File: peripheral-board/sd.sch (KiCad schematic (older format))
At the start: 0 parts

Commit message: keyboard switches and diodes placed
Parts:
- added CON7001: SD_Card, symbol SD_Card
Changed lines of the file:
@@
 $Descr A4 11693 8268
 encoding utf-8
-Sheet 1 9
+Sheet 7 9
 Title ""
 Date ""
@@
 Comment4 ""
 $EndDescr
+$Comp
+L SD_Card CON7001
+U 1 1 581F6986
+P 5750 3400
+F 0 "CON7001" H 5750 4155 50  0000 C CNN
+F 1 "SD_Card" H 5750 4064 50  0000 C CNN
+F 2 "" H 5750 3973 50  0001 C CNN
+F 3 "" H 5750 3400 50  0000 C CNN
+	1    5750 3400
+	1    0    0    -1
+$EndComp
 $EndSCHEMATC

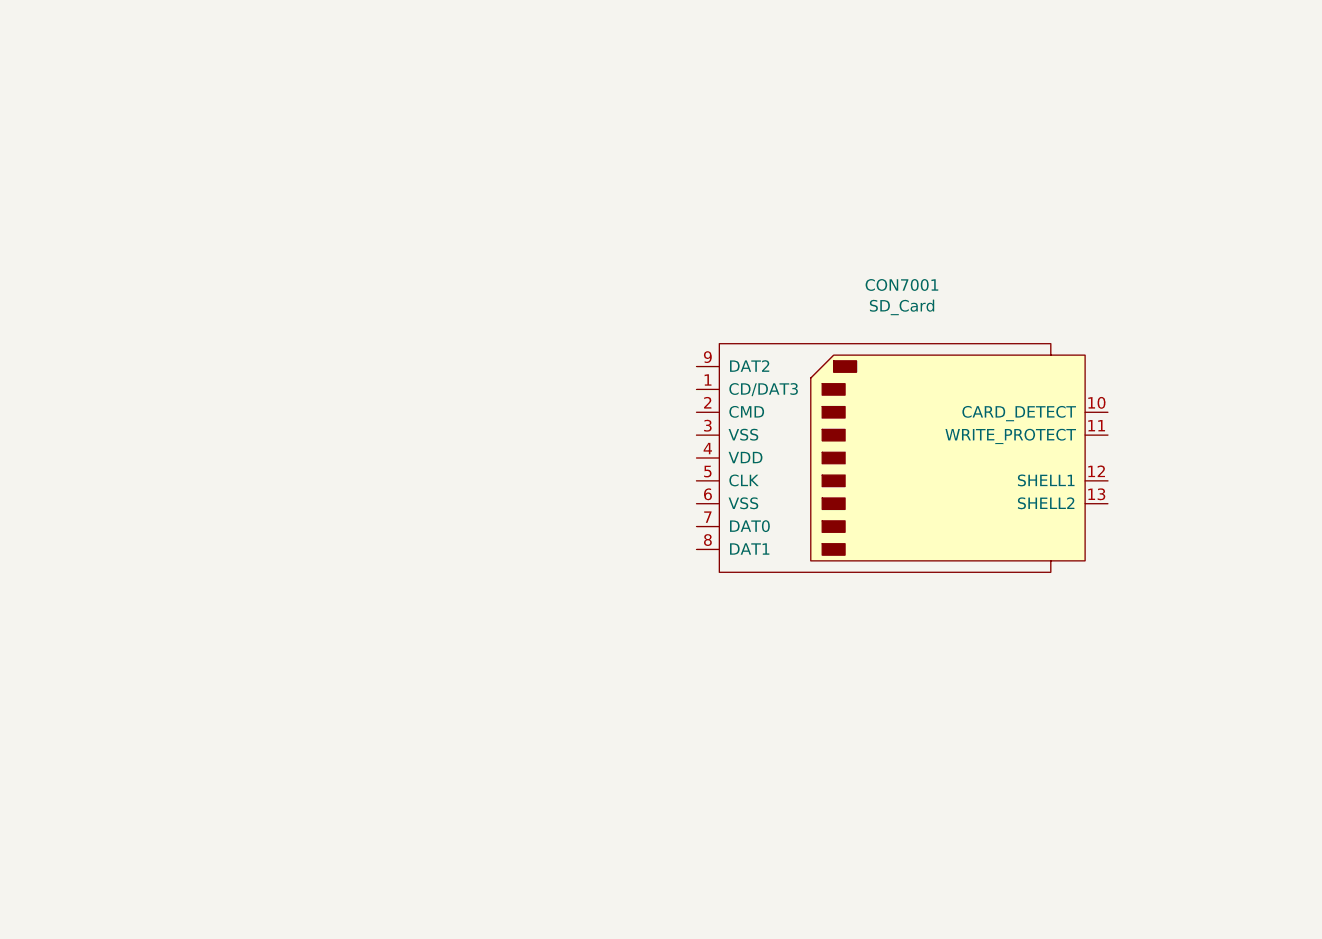
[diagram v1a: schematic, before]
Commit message: routed keyboard
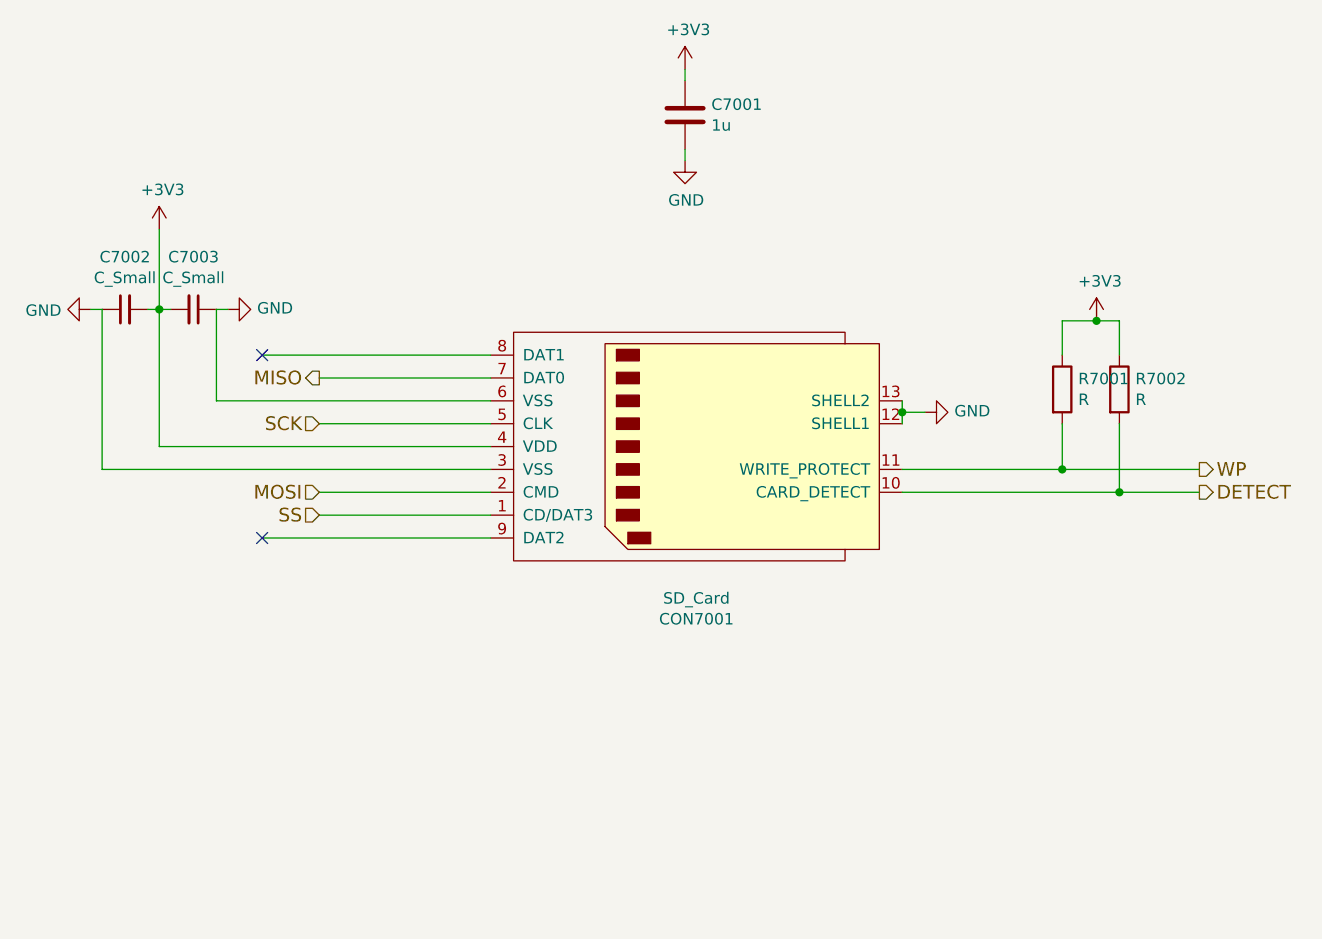
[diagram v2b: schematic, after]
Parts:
- added C7001: 1u, symbol C
- added C7002, C7003: C_Small, symbol C_Small
- added R7001, R7002: R, symbol R
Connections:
- net SS: now reaches CON7001.1 (CD/DAT3)
- net DETECT: now reaches CON7001.10 (CARD_DETECT)
- net DETECT: now also R7002.2
- net WP: now reaches CON7001.11 (WRITE_PROTECT)
- net WP: now also R7001.2
- net GND: now reaches CON7001.12 (SHELL1)
- net GND: now also CON7001.13 (SHELL2), CON7001.3 (VSS), CON7001.6 (VSS), C7001.2, C7002.1, C7003.1
- net MOSI: now reaches CON7001.2 (CMD)
- net +3V3: now reaches CON7001.4 (VDD)
- net +3V3: now also C7001.1, C7002.2, C7003.2, R7001.1, R7002.1
- net SCK: now reaches CON7001.5 (CLK)
- net MISO: now reaches CON7001.7 (DAT0)
- no-connect marks 0 -> 2
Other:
- moved on the sheet: CON7001
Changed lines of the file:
@@
 LIBS:amp
 LIBS:card-edge
+LIBS:switchmode
+LIBS:joystick
 LIBS:peripheral-board-cache
 EELAYER 25 0
@@
 L SD_Card CON7001
 U 1 1 581F6986
-P 5750 3400
-F 0 "CON7001" H 5750 4155 50  0000 C CNN
-F 1 "SD_Card" H 5750 4064 50  0000 C CNN
-F 2 "" H 5750 3973 50  0001 C CNN
-F 3 "" H 5750 3400 50  0000 C CNN
-	1    5750 3400
-	1    0    0    -1
-$EndComp
+P 4850 3350
+F 0 "CON7001" H 4850 4105 50  0000 C CNN
+F 1 "SD_Card" H 4850 4014 50  0000 C CNN
+F 2 "" H 4850 3923 50  0001 C CNN
+F 3 "" H 4850 3350 50  0000 C CNN
+	1    4850 3350
+	1    0    0    1
+$EndComp
+Wire Wire Line
+	3950 2950 2950 2950
+Wire Wire Line
+	2750 3150 3950 3150
+Wire Wire Line
+	2500 3350 3950 3350
+Wire Wire Line
+	2250 3450 3950 3450
+Wire Wire Line
+	3950 3750 2950 3750
+NoConn ~ 2950 2950
+NoConn ~ 2950 3750
+$Comp
+L C_Small C7003
+U 1 1 58222516
+P 2650 2750
+F 0 "C7003" V 2879 2750 50  0000 C CNN
+F 1 "C_Small" V 2788 2750 50  0000 C CNN
+F 2 "" H 2650 2750 50  0000 C CNN
+F 3 "" H 2650 2750 50  0000 C CNN
+	1    2650 2750
+	0    1    -1   0
+$EndComp
+$Comp
+L C_Small C7002
+U 1 1 582225EF
+P 2350 2750
+F 0 "C7002" V 2121 2750 50  0000 C CNN
+F 1 "C_Small" V 2212 2750 50  0000 C CNN
+F 2 "" H 2350 2750 50  0000 C CNN
+F 3 "" H 2350 2750 50  0000 C CNN
+	1    2350 2750
+	0    -1   1    0
+$EndComp
+Wire Wire Line
+	2750 3150 2750 2750
+Wire Wire Line
+	2250 3450 2250 2750
+Wire Wire Line
+	2550 2750 2450 2750
+Wire Wire Line
+	2500 2400 2500 3350
+Connection ~ 2500 2750
+Text HLabel 3200 3050 0    60   Output ~ 0
+MISO
+Text HLabel 3200 3550 0    60   Input ~ 0
+MOSI
+Text HLabel 3200 3650 0    60   Input ~ 0
+SS
+Text HLabel 3200 3250 0    60   Input ~ 0
+SCK
+Wire Wire Line
+	3950 3050 3200 3050
+Wire Wire Line
+	3950 3250 3200 3250
+Wire Wire Line
+	3950 3550 3200 3550
+Wire Wire Line
+	3950 3650 3200 3650
+$Comp
+L +3V3 #PWR028
+U 1 1 582229DC
+P 2500 2400
+F 0 "#PWR028" H 2500 2250 50  0001 C CNN
+F 1 "+3V3" H 2515 2573 50  0000 C CNN
+F 2 "" H 2500 2400 50  0000 C CNN
+F 3 "" H 2500 2400 50  0000 C CNN
+	1    2500 2400
+	1    0    0    -1
+$EndComp
+$Comp
+L GND #PWR029
+U 1 1 582229F6
+P 2800 2750
+F 0 "#PWR029" H 2800 2500 50  0001 C CNN
+F 1 "GND" V 2805 2622 50  0000 R CNN
+F 2 "" H 2800 2750 50  0000 C CNN
+F 3 "" H 2800 2750 50  0000 C CNN
+	1    2800 2750
+	0    -1   -1   0
+$EndComp
+$Comp
+L GND #PWR030
+U 1 1 58222A19
+P 2200 2750
+F 0 "#PWR030" H 2200 2500 50  0001 C CNN
+F 1 "GND" V 2205 2622 50  0000 R CNN
+F 2 "" H 2200 2750 50  0000 C CNN
+F 3 "" H 2200 2750 50  0000 C CNN
+	1    2200 2750
+	0    1    1    0
+$EndComp
+Wire Wire Line
+	2750 2750 2800 2750
+Wire Wire Line
+	2250 2750 2200 2750
+$Comp
+L C C7001
+U 1 1 58222A8C
+P 4800 1900
+F 0 "C7001" H 4915 1946 50  0000 L CNN
+F 1 "1u" H 4915 1855 50  0000 L CNN
+F 2 "" H 4838 1750 50  0000 C CNN
+F 3 "" H 4800 1900 50  0000 C CNN
+	1    4800 1900
+	1    0    0    -1
+$EndComp
+$Comp
+L GND #PWR031
+U 1 1 58222AC6
+P 4800 2100
+F 0 "#PWR031" H 4800 1850 50  0001 C CNN
+F 1 "GND" H 4805 1927 50  0000 C CNN
+F 2 "" H 4800 2100 50  0000 C CNN
+F 3 "" H 4800 2100 50  0000 C CNN
+	1    4800 2100
+	1    0    0    -1
+$EndComp
+$Comp
+L +3V3 #PWR032
+U 1 1 58222AE2
+P 4800 1700
+F 0 "#PWR032" H 4800 1550 50  0001 C CNN
+F 1 "+3V3" H 4815 1873 50  0000 C CNN
+F 2 "" H 4800 1700 50  0000 C CNN
+F 3 "" H 4800 1700 50  0000 C CNN
+	1    4800 1700
+	1    0    0    -1
+$EndComp
+Wire Wire Line
+	4800 1700 4800 1750
+Wire Wire Line
+	4800 2050 4800 2100
+$Comp
+L GND #PWR033
+U 1 1 58222B2D
+P 5850 3200
+F 0 "#PWR033" H 5850 2950 50  0001 C CNN
+F 1 "GND" V 5855 3072 50  0000 R CNN
+F 2 "" H 5850 3200 50  0000 C CNN
+F 3 "" H 5850 3200 50  0000 C CNN
+	1    5850 3200
+	0    -1   -1   0
+$EndComp
+Wire Wire Line
+	5750 3150 5750 3250
+Wire Wire Line
+	5750 3200 5850 3200
+Connection ~ 5750 3200
+Text HLabel 7050 3450 2    60   Output ~ 0
+WP
+Text HLabel 7050 3550 2    60   Output ~ 0
+DETECT
+Wire Wire Line
+	5750 3450 7050 3450
+Wire Wire Line
+	5750 3550 7050 3550
+$Comp
+L R R7001
+U 1 1 582234E6
+P 6450 3100
+F 0 "R7001" H 6520 3146 50  0000 L CNN
+F 1 "R" H 6520 3055 50  0000 L CNN
+F 2 "" V 6380 3100 50  0000 C CNN
+F 3 "" H 6450 3100 50  0000 C CNN
+	1    6450 3100
+	1    0    0    -1
+$EndComp
+$Comp
+L R R7002
+U 1 1 5822353B
+P 6700 3100
+F 0 "R7002" H 6770 3146 50  0000 L CNN
+F 1 "R" H 6770 3055 50  0000 L CNN
+F 2 "" V 6630 3100 50  0000 C CNN
+F 3 "" H 6700 3100 50  0000 C CNN
+	1    6700 3100
+	1    0    0    -1
+$EndComp
+Wire Wire Line
+	6700 3550 6700 3250
+Connection ~ 6700 3550
+Wire Wire Line
+	6450 3250 6450 3450
+Connection ~ 6450 3450
+$Comp
+L +3V3 #PWR034
+U 1 1 582235F2
+P 6600 2800
+F 0 "#PWR034" H 6600 2650 50  0001 C CNN
+F 1 "+3V3" H 6615 2973 50  0000 C CNN
+F 2 "" H 6600 2800 50  0000 C CNN
+F 3 "" H 6600 2800 50  0000 C CNN
+	1    6600 2800
+	1    0    0    -1
+$EndComp
+Wire Wire Line
+	6700 2800 6700 2950
+Wire Wire Line
+	6450 2800 6700 2800
+Wire Wire Line
+	6450 2800 6450 2950
+Connection ~ 6600 2800
 $EndSCHEMATC

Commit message: added some audio circuitry
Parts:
- C7001: footprint (none) -> Capacitors_SMD:C_1206
- C7002, C7003: footprint (none) -> Capacitors_SMD:C_0805
- CON7001: footprint (none) -> lib:TS-2198-01
- R7001, R7002: footprint (none) -> Resistors_SMD:R_0805
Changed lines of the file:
@@
 LIBS:switchmode
 LIBS:joystick
+LIBS:digital-pot
 LIBS:peripheral-board-cache
-EELAYER 25 0
+EELAYER 26 0
 EELAYER END
 $Descr A4 11693 8268
@@
 F 0 "CON7001" H 4850 4105 50  0000 C CNN
 F 1 "SD_Card" H 4850 4014 50  0000 C CNN
-F 2 "" H 4850 3923 50  0001 C CNN
+F 2 "lib:TS-2198-01" H 4850 3923 50  0001 C CNN
 F 3 "" H 4850 3350 50  0000 C CNN
 	1    4850 3350
@@
 F 0 "C7003" V 2879 2750 50  0000 C CNN
 F 1 "C_Small" V 2788 2750 50  0000 C CNN
-F 2 "" H 2650 2750 50  0000 C CNN
+F 2 "Capacitors_SMD:C_0805" H 2650 2750 50  0001 C CNN
 F 3 "" H 2650 2750 50  0000 C CNN
 	1    2650 2750
@@
 F 0 "C7002" V 2121 2750 50  0000 C CNN
 F 1 "C_Small" V 2212 2750 50  0000 C CNN
-F 2 "" H 2350 2750 50  0000 C CNN
+F 2 "Capacitors_SMD:C_0805" H 2350 2750 50  0001 C CNN
 F 3 "" H 2350 2750 50  0000 C CNN
 	1    2350 2750
@@
 	3950 3650 3200 3650
 $Comp
-L +3V3 #PWR028
+L +3V3 #PWR034
 U 1 1 582229DC
 P 2500 2400
-F 0 "#PWR028" H 2500 2250 50  0001 C CNN
+F 0 "#PWR034" H 2500 2250 50  0001 C CNN
 F 1 "+3V3" H 2515 2573 50  0000 C CNN
 F 2 "" H 2500 2400 50  0000 C CNN
@@
 $EndComp
 $Comp
-L GND #PWR029
+L GND #PWR035
 U 1 1 582229F6
 P 2800 2750
-F 0 "#PWR029" H 2800 2500 50  0001 C CNN
+F 0 "#PWR035" H 2800 2500 50  0001 C CNN
 F 1 "GND" V 2805 2622 50  0000 R CNN
 F 2 "" H 2800 2750 50  0000 C CNN
@@
 $EndComp
 $Comp
-L GND #PWR030
+L GND #PWR036
 U 1 1 58222A19
 P 2200 2750
-F 0 "#PWR030" H 2200 2500 50  0001 C CNN
+F 0 "#PWR036" H 2200 2500 50  0001 C CNN
 F 1 "GND" V 2205 2622 50  0000 R CNN
 F 2 "" H 2200 2750 50  0000 C CNN
@@
 F 0 "C7001" H 4915 1946 50  0000 L CNN
 F 1 "1u" H 4915 1855 50  0000 L CNN
-F 2 "" H 4838 1750 50  0000 C CNN
+F 2 "Capacitors_SMD:C_1206" H 4838 1750 50  0001 C CNN
 F 3 "" H 4800 1900 50  0000 C CNN
 	1    4800 1900
@@
 $EndComp
 $Comp
-L GND #PWR031
+L GND #PWR037
 U 1 1 58222AC6
 P 4800 2100
-F 0 "#PWR031" H 4800 1850 50  0001 C CNN
+F 0 "#PWR037" H 4800 1850 50  0001 C CNN
 F 1 "GND" H 4805 1927 50  0000 C CNN
 F 2 "" H 4800 2100 50  0000 C CNN
@@
 $EndComp
 $Comp
-L +3V3 #PWR032
+L +3V3 #PWR038
 U 1 1 58222AE2
 P 4800 1700
-F 0 "#PWR032" H 4800 1550 50  0001 C CNN
+F 0 "#PWR038" H 4800 1550 50  0001 C CNN
 F 1 "+3V3" H 4815 1873 50  0000 C CNN
 F 2 "" H 4800 1700 50  0000 C CNN
@@
 	4800 2050 4800 2100
 $Comp
-L GND #PWR033
+L GND #PWR039
 U 1 1 58222B2D
 P 5850 3200
-F 0 "#PWR033" H 5850 2950 50  0001 C CNN
+F 0 "#PWR039" H 5850 2950 50  0001 C CNN
 F 1 "GND" V 5855 3072 50  0000 R CNN
 F 2 "" H 5850 3200 50  0000 C CNN
@@
 F 0 "R7001" H 6520 3146 50  0000 L CNN
 F 1 "R" H 6520 3055 50  0000 L CNN
-F 2 "" V 6380 3100 50  0000 C CNN
+F 2 "Resistors_SMD:R_0805" V 6380 3100 50  0001 C CNN
 F 3 "" H 6450 3100 50  0000 C CNN
 	1    6450 3100
@@
 F 0 "R7002" H 6770 3146 50  0000 L CNN
 F 1 "R" H 6770 3055 50  0000 L CNN
-F 2 "" V 6630 3100 50  0000 C CNN
+F 2 "Resistors_SMD:R_0805" V 6630 3100 50  0001 C CNN
 F 3 "" H 6700 3100 50  0000 C CNN
 	1    6700 3100
@@
 Connection ~ 6450 3450
 $Comp
-L +3V3 #PWR034
+L +3V3 #PWR040
 U 1 1 582235F2
 P 6600 2800
-F 0 "#PWR034" H 6600 2650 50  0001 C CNN
+F 0 "#PWR040" H 6600 2650 50  0001 C CNN
 F 1 "+3V3" H 6615 2973 50  0000 C CNN
 F 2 "" H 6600 2800 50  0000 C CNN

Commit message: audio circuitry
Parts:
- C8002: renamed from C7001; footprint Capacitors_SMD:C_1206 -> Capacitors_SMD:C_0805
- C8003: renamed from C7002; value C_Small -> 100n
- C8004: renamed from C7003; value C_Small -> 100n
- R8001: renamed from R7001; value R -> 47k
- R8002: renamed from R7002; value R -> 47k
- renumbered CON7001 to CON8001
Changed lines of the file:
@@
 EESchema Schematic File Version 2
+LIBS:peripheral-board-rescue
 LIBS:power
 LIBS:device
@@
 LIBS:digital-pot
 LIBS:vref
+LIBS:switches
 LIBS:peripheral-board-cache
 EELAYER 26 0
@@
 $Descr A4 11693 8268
 encoding utf-8
-Sheet 7 10
+Sheet 8 10
 Title ""
 Date ""
@@
 $EndDescr
 $Comp
-L SD_Card CON7001
+L SD_Card CON8001
 U 1 1 581F6986
 P 4850 3350
-F 0 "CON7001" H 4850 4105 50  0000 C CNN
+F 0 "CON8001" H 4850 4105 50  0000 C CNN
 F 1 "SD_Card" H 4850 4014 50  0000 C CNN
 F 2 "lib:TS-2198-01" H 4850 3923 50  0001 C CNN
@@
 NoConn ~ 2950 3750
 $Comp
-L C_Small C7003
+L C_Small C8004
 U 1 1 58222516
 P 2650 2750
-F 0 "C7003" V 2879 2750 50  0000 C CNN
-F 1 "C_Small" V 2788 2750 50  0000 C CNN
+F 0 "C8004" V 2879 2750 50  0000 C CNN
+F 1 "100n" V 2788 2750 50  0000 C CNN
 F 2 "Capacitors_SMD:C_0805" H 2650 2750 50  0001 C CNN
 F 3 "" H 2650 2750 50  0000 C CNN
@@
 $EndComp
 $Comp
-L C_Small C7002
+L C_Small C8003
 U 1 1 582225EF
 P 2350 2750
-F 0 "C7002" V 2121 2750 50  0000 C CNN
-F 1 "C_Small" V 2212 2750 50  0000 C CNN
+F 0 "C8003" V 2121 2750 50  0000 C CNN
+F 1 "100n" V 2212 2750 50  0000 C CNN
 F 2 "Capacitors_SMD:C_0805" H 2350 2750 50  0001 C CNN
 F 3 "" H 2350 2750 50  0000 C CNN
@@
 	3950 3650 3200 3650
 $Comp
-L +3V3 #PWR060
+L +3V3 #PWR8003
 U 1 1 582229DC
 P 2500 2400
-F 0 "#PWR060" H 2500 2250 50  0001 C CNN
+F 0 "#PWR8003" H 2500 2250 50  0001 C CNN
 F 1 "+3V3" H 2515 2573 50  0000 C CNN
 F 2 "" H 2500 2400 50  0000 C CNN
@@
 $EndComp
 $Comp
-L GND #PWR061
+L GND #PWR8005
 U 1 1 582229F6
 P 2800 2750
-F 0 "#PWR061" H 2800 2500 50  0001 C CNN
+F 0 "#PWR8005" H 2800 2500 50  0001 C CNN
 F 1 "GND" V 2805 2622 50  0000 R CNN
 F 2 "" H 2800 2750 50  0000 C CNN
@@
 $EndComp
 $Comp
-L GND #PWR062
+L GND #PWR8004
 U 1 1 58222A19
 P 2200 2750
-F 0 "#PWR062" H 2200 2500 50  0001 C CNN
+F 0 "#PWR8004" H 2200 2500 50  0001 C CNN
 F 1 "GND" V 2205 2622 50  0000 R CNN
 F 2 "" H 2200 2750 50  0000 C CNN
@@
 	2250 2750 2200 2750
 $Comp
-L C C7001
+L C C8002
 U 1 1 58222A8C
 P 4800 1900
-F 0 "C7001" H 4915 1946 50  0000 L CNN
+F 0 "C8002" H 4915 1946 50  0000 L CNN
 F 1 "1u" H 4915 1855 50  0000 L CNN
-F 2 "Capacitors_SMD:C_1206" H 4838 1750 50  0001 C CNN
+F 2 "Capacitors_SMD:C_0805" H 4838 1750 50  0001 C CNN
 F 3 "" H 4800 1900 50  0000 C CNN
 	1    4800 1900
@@
 $EndComp
 $Comp
-L GND #PWR063
+L GND #PWR8002
 U 1 1 58222AC6
 P 4800 2100
-F 0 "#PWR063" H 4800 1850 50  0001 C CNN
+F 0 "#PWR8002" H 4800 1850 50  0001 C CNN
 F 1 "GND" H 4805 1927 50  0000 C CNN
 F 2 "" H 4800 2100 50  0000 C CNN
@@
 $EndComp
 $Comp
-L +3V3 #PWR064
+L +3V3 #PWR8001
 U 1 1 58222AE2
 P 4800 1700
-F 0 "#PWR064" H 4800 1550 50  0001 C CNN
+F 0 "#PWR8001" H 4800 1550 50  0001 C CNN
 F 1 "+3V3" H 4815 1873 50  0000 C CNN
 F 2 "" H 4800 1700 50  0000 C CNN
@@
 	4800 2050 4800 2100
 $Comp
-L GND #PWR065
+L GND #PWR8007
 U 1 1 58222B2D
 P 5850 3200
-F 0 "#PWR065" H 5850 2950 50  0001 C CNN
+F 0 "#PWR8007" H 5850 2950 50  0001 C CNN
 F 1 "GND" V 5855 3072 50  0000 R CNN
 F 2 "" H 5850 3200 50  0000 C CNN
@@
 	5750 3550 7050 3550
 $Comp
-L R R7001
+L R R8001
 U 1 1 582234E6
 P 6450 3100
-F 0 "R7001" H 6520 3146 50  0000 L CNN
-F 1 "R" H 6520 3055 50  0000 L CNN
+F 0 "R8001" H 6520 3146 50  0000 L CNN
+F 1 "47k" H 6520 3055 50  0000 L CNN
 F 2 "Resistors_SMD:R_0805" V 6380 3100 50  0001 C CNN
 F 3 "" H 6450 3100 50  0000 C CNN
@@
 $EndComp
 $Comp
-L R R7002
+L R R8002
 U 1 1 5822353B
 P 6700 3100
-F 0 "R7002" H 6770 3146 50  0000 L CNN
-F 1 "R" H 6770 3055 50  0000 L CNN
+F 0 "R8002" H 6770 3146 50  0000 L CNN
+F 1 "47k" H 6770 3055 50  0000 L CNN
 F 2 "Resistors_SMD:R_0805" V 6630 3100 50  0001 C CNN
 F 3 "" H 6700 3100 50  0000 C CNN
@@
 Connection ~ 6450 3450
 $Comp
-L +3V3 #PWR066
+L +3V3 #PWR8006
 U 1 1 582235F2
 P 6600 2800
-F 0 "#PWR066" H 6600 2650 50  0001 C CNN
+F 0 "#PWR8006" H 6600 2650 50  0001 C CNN
 F 1 "+3V3" H 6615 2973 50  0000 C CNN
 F 2 "" H 6600 2800 50  0000 C CNN

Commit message: routed spi
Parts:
- added D8001: LED_SD, LEDs:LED-3MM, symbol LED
- added Q8001: BSS84LT1G, TO_SOT_Packages_SMD:SOT-23, symbol Q_PMOS_GSD
- added R8003: 1k, Resistors_SMD:R_0805, symbol R
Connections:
- net +3V3: now also Q8001.2 (S)
- net GND: now also R8003.1
- net SS: now also Q8001.1 (G)
- new net: D8001.1 (K), R8003.2
- new net: D8001.2 (A), Q8001.3 (D)
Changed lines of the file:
@@
 $EndComp
-Wire Wire Line
-	3950 2950 2950 2950
 Wire Wire Line
 	2750 3150 3950 3150
@@
 Wire Wire Line
 	2250 3450 3950 3450
-Wire Wire Line
-	3950 3750 2950 3750
-NoConn ~ 2950 2950
-NoConn ~ 2950 3750
+NoConn ~ 3950 2950
+NoConn ~ 3950 3750
 $Comp
 L C_Small C8004
@@
 	3950 3650 3200 3650
 $Comp
-L +3V3 #PWR075
+L +3V3 #PWR077
 U 1 1 582229DC
 P 2500 2400
-F 0 "#PWR075" H 2500 2250 50  0001 C CNN
+F 0 "#PWR077" H 2500 2250 50  0001 C CNN
 F 1 "+3V3" H 2515 2573 50  0000 C CNN
 F 2 "" H 2500 2400 50  0000 C CNN
@@
 $EndComp
 $Comp
-L GND #PWR076
+L GND #PWR078
 U 1 1 582229F6
 P 2800 2750
-F 0 "#PWR076" H 2800 2500 50  0001 C CNN
+F 0 "#PWR078" H 2800 2500 50  0001 C CNN
 F 1 "GND" V 2805 2622 50  0000 R CNN
 F 2 "" H 2800 2750 50  0000 C CNN
@@
 $EndComp
 $Comp
-L GND #PWR077
+L GND #PWR079
 U 1 1 58222A19
 P 2200 2750
-F 0 "#PWR077" H 2200 2500 50  0001 C CNN
+F 0 "#PWR079" H 2200 2500 50  0001 C CNN
 F 1 "GND" V 2205 2622 50  0000 R CNN
 F 2 "" H 2200 2750 50  0000 C CNN
@@
 $EndComp
 $Comp
-L GND #PWR078
+L GND #PWR080
 U 1 1 58222AC6
 P 4800 2100
-F 0 "#PWR078" H 4800 1850 50  0001 C CNN
+F 0 "#PWR080" H 4800 1850 50  0001 C CNN
 F 1 "GND" H 4805 1927 50  0000 C CNN
 F 2 "" H 4800 2100 50  0000 C CNN
@@
 $EndComp
 $Comp
-L +3V3 #PWR079
+L +3V3 #PWR081
 U 1 1 58222AE2
 P 4800 1700
-F 0 "#PWR079" H 4800 1550 50  0001 C CNN
+F 0 "#PWR081" H 4800 1550 50  0001 C CNN
 F 1 "+3V3" H 4815 1873 50  0000 C CNN
 F 2 "" H 4800 1700 50  0000 C CNN
@@
 	4800 2050 4800 2100
 $Comp
-L GND #PWR080
+L GND #PWR082
 U 1 1 58222B2D
 P 5850 3200
-F 0 "#PWR080" H 5850 2950 50  0001 C CNN
+F 0 "#PWR082" H 5850 2950 50  0001 C CNN
 F 1 "GND" V 5855 3072 50  0000 R CNN
 F 2 "" H 5850 3200 50  0000 C CNN
@@
 Connection ~ 6450 3450
 $Comp
-L +3V3 #PWR081
+L +3V3 #PWR083
 U 1 1 582235F2
 P 6600 2800
-F 0 "#PWR081" H 6600 2650 50  0001 C CNN
+F 0 "#PWR083" H 6600 2650 50  0001 C CNN
 F 1 "+3V3" H 6615 2973 50  0000 C CNN
 F 2 "" H 6600 2800 50  0000 C CNN
@@
 	6450 2800 6450 2950
 Connection ~ 6600 2800
+$Comp
+L LED D8001
+U 1 1 58A4E82B
+P 3700 4750
+F 0 "D8001" V 3738 4632 50  0000 R CNN
+F 1 "LED_SD" V 3647 4632 50  0000 R CNN
+F 2 "LEDs:LED-3MM" H 1100 2900 50  0001 C CNN
+F 3 "" H 1100 2900 50  0001 C CNN
+	1    3700 4750
+	0    -1   -1   0
+$EndComp
+$Comp
+L R R8003
+U 1 1 58A4E890
+P 3700 5050
+F 0 "R8003" H 3630 5004 50  0000 R CNN
+F 1 "1k" H 3630 5095 50  0000 R CNN
+F 2 "Resistors_SMD:R_0805" V -270 250 50  0001 C CNN
+F 3 "" H -200 250 50  0001 C CNN
+	1    3700 5050
+	-1   0    0    1
+$EndComp
+$Comp
+L Q_PMOS_GSD Q8001
+U 1 1 58A4E972
+P 3600 4400
+F 0 "Q8001" H 3806 4354 50  0000 L CNN
+F 1 "BSS84LT1G" H 3806 4445 50  0000 L CNN
+F 2 "TO_SOT_Packages_SMD:SOT-23" H 2400 450 50  0001 C CNN
+F 3 "" H 2200 350 50  0001 C CNN
+	1    3600 4400
+	1    0    0    1
+$EndComp
+$Comp
+L GND #PWR084
+U 1 1 58A4EBF7
+P 3700 5200
+F 0 "#PWR084" H 1950 200 50  0001 C CNN
+F 1 "GND" H 3705 5027 50  0000 C CNN
+F 2 "" H 1950 450 50  0001 C CNN
+F 3 "" H 1950 450 50  0001 C CNN
+	1    3700 5200
+	1    0    0    -1
+$EndComp
+$Comp
+L +3V3 #PWR085
+U 1 1 58A4ED0D
+P 3700 4200
+F 0 "#PWR085" H 1650 100 50  0001 C CNN
+F 1 "+3V3" H 3715 4373 50  0000 C CNN
+F 2 "" H 1650 250 50  0001 C CNN
+F 3 "" H 1650 250 50  0001 C CNN
+	1    3700 4200
+	1    0    0    -1
+$EndComp
+Wire Wire Line
+	3250 3650 3250 4400
+Wire Wire Line
+	3250 4400 3400 4400
+Connection ~ 3250 3650
 $EndSCHEMATC
